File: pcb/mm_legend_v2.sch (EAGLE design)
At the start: 74 parts, among them IC1 ULN2003AD, IC2 TB6612FNG

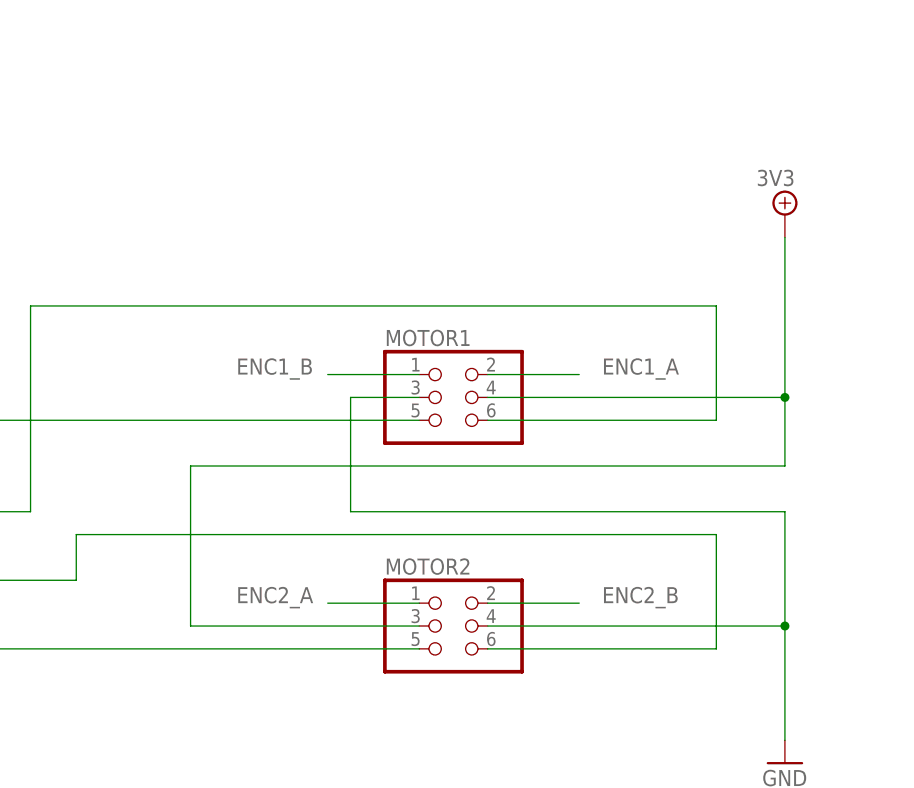
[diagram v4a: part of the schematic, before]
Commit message: pcb: fix motor connector wiring.
Fix issue #1.
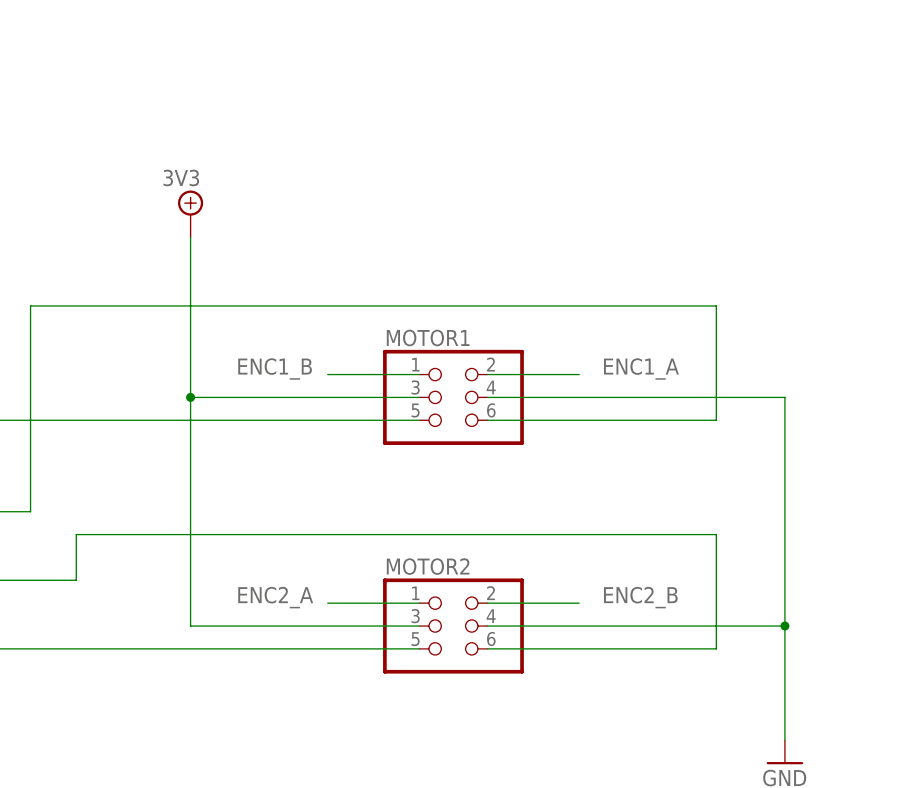
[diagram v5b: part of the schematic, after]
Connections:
- net 3V3: now also MOTOR1.3; no longer MOTOR1.4
- net GND: now also MOTOR1.4; no longer MOTOR1.3
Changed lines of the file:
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@@
 <instance part="SUPPLY31" gate="G$1" x="330.2" y="157.48"/>
 <instance part="SUPPLY32" gate="G$1" x="365.76" y="157.48"/>
-<instance part="SUPPLY26" gate="G$1" x="375.92" y="17.78"/>
+<instance part="SUPPLY26" gate="G$1" x="309.88" y="17.78"/>
 </instances>
 <busses>
@@
 <wire x1="342.9" y1="-27.94" x2="375.92" y2="-27.94" width="0.1524" layer="91"/>
 <wire x1="375.92" y1="-27.94" x2="375.92" y2="-40.64" width="0.1524" layer="91"/>
-<wire x1="375.92" y1="-27.94" x2="375.92" y2="-15.24" width="0.1524" layer="91"/>
-<wire x1="375.92" y1="-15.24" x2="327.66" y2="-15.24" width="0.1524" layer="91"/>
-<wire x1="327.66" y1="-15.24" x2="327.66" y2="-2.54" width="0.1524" layer="91"/>
-<pinref part="MOTOR1" gate="A" pin="3"/>
-<wire x1="327.66" y1="-2.54" x2="335.28" y2="-2.54" width="0.1524" layer="91"/>
 <junction x="375.92" y="-27.94"/>
+<pinref part="MOTOR1" gate="A" pin="4"/>
+<wire x1="342.9" y1="-2.54" x2="375.92" y2="-2.54" width="0.1524" layer="91"/>
+<wire x1="375.92" y1="-2.54" x2="375.92" y2="-27.94" width="0.1524" layer="91"/>
 </segment>
 </net>
@@
 <segment>
 <pinref part="SUPPLY26" gate="G$1" pin="+5V/1"/>
-<wire x1="375.92" y1="15.24" x2="375.92" y2="-2.54" width="0.1524" layer="91"/>
-<pinref part="MOTOR1" gate="A" pin="4"/>
-<wire x1="375.92" y1="-2.54" x2="342.9" y2="-2.54" width="0.1524" layer="91"/>
 <pinref part="MOTOR2" gate="A" pin="3"/>
 <wire x1="335.28" y1="-27.94" x2="309.88" y2="-27.94" width="0.1524" layer="91"/>
-<wire x1="309.88" y1="-27.94" x2="309.88" y2="-10.16" width="0.1524" layer="91"/>
-<wire x1="309.88" y1="-10.16" x2="375.92" y2="-10.16" width="0.1524" layer="91"/>
-<wire x1="375.92" y1="-10.16" x2="375.92" y2="-2.54" width="0.1524" layer="91"/>
-<junction x="375.92" y="-2.54"/>
-</segment>
-</net>
+<wire x1="309.88" y1="-27.94" x2="309.88" y2="-2.54" width="0.1524" layer="91"/>
+<pinref part="MOTOR1" gate="A" pin="3"/>
+<wire x1="309.88" y1="-2.54" x2="309.88" y2="15.24" width="0.1524" layer="91"/>
+<wire x1="335.28" y1="-2.54" x2="309.88" y2="-2.54" width="0.1524" layer="91"/>
+<junction x="309.88" y="-2.54"/>
+</segment>
+</net>
